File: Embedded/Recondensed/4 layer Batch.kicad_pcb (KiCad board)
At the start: 4 copper layers, 60 x 89.5 mm, 91 parts, among them J1 10171746-00021LF, J10 Fan 1, J11 Substructure Power, J12 Head Power, J13 MicroSD, J14 Mic, J15 Expansion, J2 HUB75 Right, J2 LEDs 0, J3 Display Power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

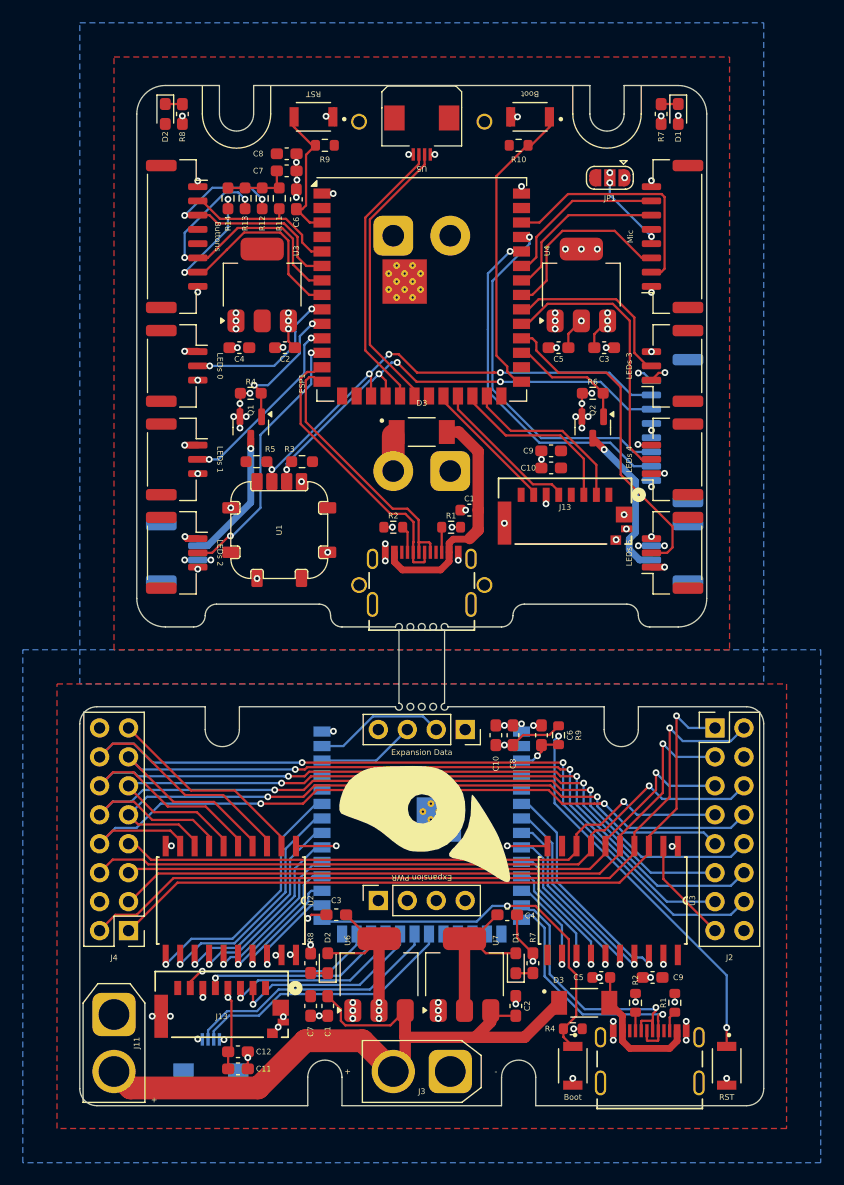
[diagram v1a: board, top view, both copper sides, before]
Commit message: Modified Batch to be Production Ready
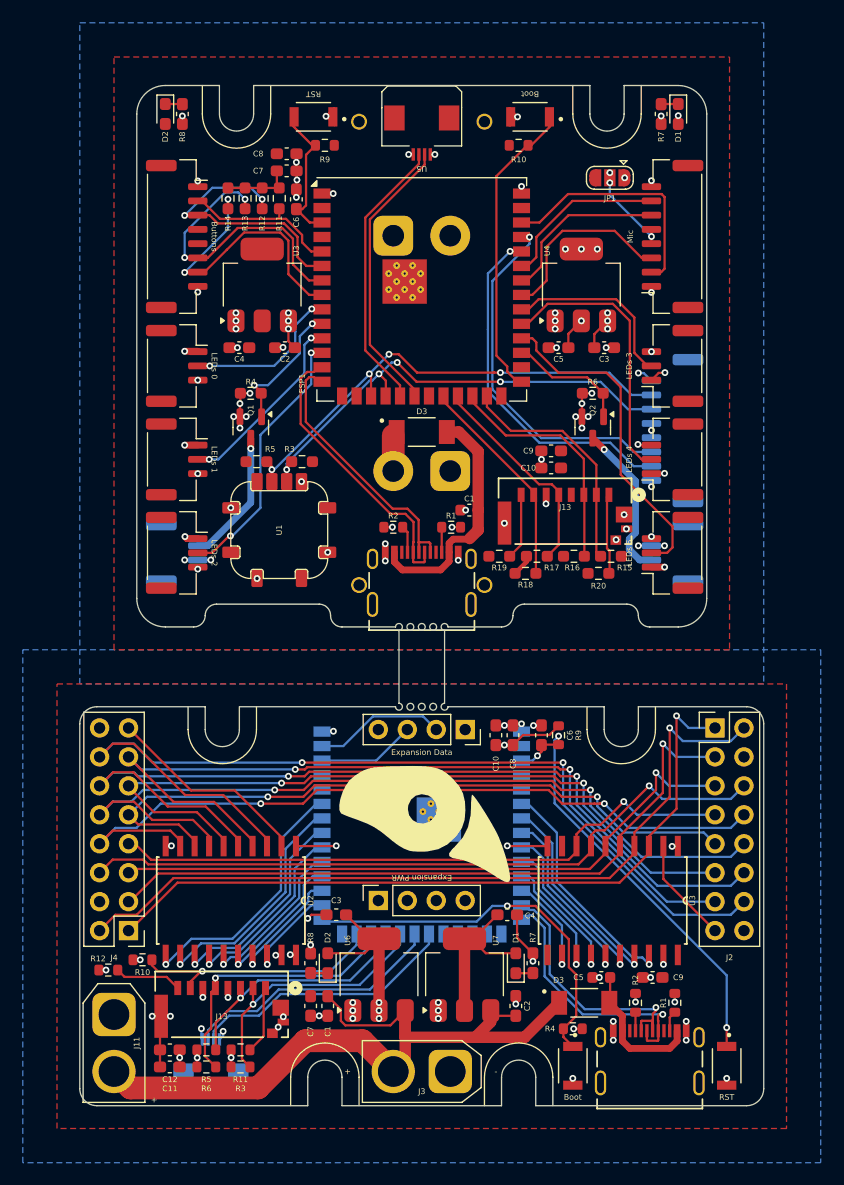
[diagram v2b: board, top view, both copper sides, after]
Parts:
- added R10: 10K, Resistor_SMD:R_0603_1608Metric, F.Cu at (125.5, 132.2)
- added R11: 10K, Resistor_SMD:R_0603_1608Metric, F.Cu at (134.1, 140.1)
- added R12: 10K, Resistor_SMD:R_0603_1608Metric, F.Cu at (122.5, 133.1)
- added R15: 10K, Resistor_SMD:R_0603_1608Metric_Pad0.98x0.95mm_HandSolder, F.Cu at (166.6, 96.8)
- added R16: 10K, Resistor_SMD:R_0603_1608Metric_Pad0.98x0.95mm_HandSolder, F.Cu at (163.3, 96.8)
- added R17: 10K, Resistor_SMD:R_0603_1608Metric_Pad0.98x0.95mm_HandSolder, F.Cu at (160.1, 96.8)
- added R18: 10K, Resistor_SMD:R_0603_1608Metric_Pad0.98x0.95mm_HandSolder, F.Cu at (159.1, 98.3)
- added R19: 10K, Resistor_SMD:R_0603_1608Metric_Pad0.98x0.95mm_HandSolder, F.Cu at (156.8, 96.8)
- added R20: 10K, Resistor_SMD:R_0603_1608Metric_Pad0.98x0.95mm_HandSolder, F.Cu at (165.5, 98.3)
- added R3: 10K, Resistor_SMD:R_0603_1608Metric, F.Cu at (134.1, 141.6)
- added R5: 10K, Resistor_SMD:R_0603_1608Metric, F.Cu at (131.1, 140.1)
- added R6: 10K, Resistor_SMD:R_0603_1608Metric, F.Cu at (131.1, 141.6)
- moved C11 5.98 mm to (127.9, 141.6), turned to 180 degrees
- moved C12 5.98 mm to (127.9, 140.1), turned to 180 degrees
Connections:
- J13 pad 1: unconnected-(J13-Pad1) -> Net-(J13-Pad1) (x2)
- J13 pad 8: unconnected-(J13-Pad8) -> Net-(J13-Pad8) (x2)
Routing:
- net SD SPI CLK: track 30.0 -> 43.4 mm
- net Net-(J13-Pad1): track 0.00 -> 13.1 mm
- net SD SPI MISO: track 29.4 -> 41.7 mm
- net SD SPI CS: track 32.7 -> 44.4 mm
- net Net-(J13-Pad8): track 0.00 -> 11.7 mm
- net SD SPI MOSI: track 32.0 -> 42.9 mm
- net GND: track 78.9 -> 82.4 mm, vias 98 -> 97
- net +3V3: track 37.5 -> 40.0 mm, vias 6 -> 11
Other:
- board text added: "Des: CSF-Main-CPU M/N: CSF-AAA-001 Rev: D0.0 Dat: 28.07.2025"
- board text added: "Des: CSF-Substructure-GPU M/N: CSF-AAA-000 Rev: D0.0 Dat: 28.07.2025"
- board text removed: "Des: CSF-Main-CPU M/N: CSF-AAA-001 Rev: D0.0 Dat: 27.07.2025"
- board text removed: "Des: CSF-Substructure-GPU M/N: CSF-AAA-000 Rev: D0.0 Dat: 27.07.2025"
